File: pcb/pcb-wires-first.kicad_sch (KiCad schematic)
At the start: 54 parts, among them J1 Conn_01x04, J2 Conn_01x04, J3 Conn_01x04, J4 Conn_01x02, J5 Conn_01x02, J6 Conn_01x02, J7 Conn_01x02, SW1 on-1, SW2 off-1, SW3 on-2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

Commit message: More routing.
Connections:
- net fault: now also R4.1
- net switch-3: no longer R4.1
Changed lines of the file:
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@@
 		)
 	)
-	(global_label "switch-3"
+	(global_label "fault"
 		(shape input)
 		(at 290.83 210.82 90)
@@
 		)
 		(property "Intersheetrefs" "${INTERSHEET_REFS}"
-			(at 290.83 199.1262 90)
+			(at 290.83 203.4202 90)
 			(hide yes)
 			(show_name no)

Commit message: Routed!
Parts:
- removed NT2: gnd-bridge, symbol Device:NetTie_2
- added JP1: SolderJumper_2_Bridged, Jumper:SolderJumper-2_P1.3mm_Bridged_RoundedPad1.0x1.5mm, symbol Jumper:SolderJumper_2_Bridged
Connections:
- net GND: now also JP1.2 (B)
- net HV-GND: now also JP1.1 (A)
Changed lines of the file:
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@@
+	(wire
+		(pts
+			(xy 306.07 176.53) (xy 306.07 179.07)
+		)
+		(stroke
+			(width 0)
+			(type default)
+		)
+	)
 	(wire
 		(pts
@@
 	(wire
 		(pts
+			(xy 313.69 179.07) (xy 313.69 176.53)
+		)
+		(stroke
+			(width 0)
+			(type default)
+		)
+	)
+	(wire
+		(pts
 			(xy 134.62 208.28) (xy 132.08 208.28)
 		)
@@
 		(pts
 			(xy 290.83 210.82) (xy 290.83 213.36)
+		)
+		(stroke
+			(width 0)
+			(type default)
+		)
+	)
+	(wire
+		(pts
+			(xy 313.69 176.53) (xy 316.23 176.53)
 		)
 		(stroke
@@
 	)
 	(symbol
-		(lib_id "Device:NetTie_2")
-		(at 311.15 179.07 0)
-		(unit 1)
-		(body_style 1)
-		(exclude_from_sim no)
-		(in_bom no)
-		(on_board yes)
-		(in_pos_files yes)
-		(dnp no)
-		(fields_autoplaced yes)
-		(property "Reference" "NT2"
-			(at 311.15 173.99 0)
-			(hide yes)
-			(show_name no)
-			(do_not_autoplace no)
-			(effects
-				(font
-					(size 1.27 1.27)
-				)
-			)
-		)
-		(property "Value" "gnd-bridge"
-			(at 311.15 176.53 0)
-			(hide yes)
-			(show_name no)
-			(do_not_autoplace no)
-			(effects
-				(font
-					(size 1.27 1.27)
-				)
-			)
-		)
-		(property "Footprint" ""
-			(at 311.15 179.07 0)
-			(hide yes)
-			(show_name no)
-			(do_not_autoplace no)
-			(effects
-				(font
-					(size 1.27 1.27)
-				)
-			)
-		)
-		(property "Datasheet" ""
-			(at 311.15 179.07 0)
-			(hide yes)
-			(show_name no)
-			(do_not_autoplace no)
-			(effects
-				(font
-					(size 1.27 1.27)
-				)
-			)
-		)
-		(property "Description" "Net tie, 2 pins"
-			(at 311.15 179.07 0)
-			(hide yes)
-			(show_name no)
-			(do_not_autoplace no)
-			(effects
-				(font
-					(size 1.27 1.27)
-				)
-			)
-		)
-		(pin "2"
-		)
-		(pin "1"
-		)
-		(instances
-			(project "pcb-wires-first"
-				(path "/2155cca2-5ec1-4d94-9553-ebcda519e5b5"
-					(reference "NT2")
-					(unit 1)
-				)
-			)
-		)
-	)
-	(symbol
 		(lib_id "Device:LED")
 		(at 325.12 226.06 90)
@@
 					(unit 1)
 				)
+			)
+		)
+	)
+	(symbol
+		(lib_id "Jumper:SolderJumper_2_Bridged")
+		(at 311.15 176.53 0)
+		(unit 1)
+		(body_style 1)
+		(exclude_from_sim no)
+		(in_bom no)
+		(on_board yes)
+		(in_pos_files yes)
+		(dnp no)
+		(fields_autoplaced yes)
+		(property "Reference" "JP1"
+			(at 311.15 170.18 0)
+			(show_name no)
+			(do_not_autoplace no)
+			(effects
+				(font
+					(size 1.27 1.27)
+				)
+			)
+		)
+		(property "Value" "SolderJumper_2_Bridged"
+			(at 311.15 172.72 0)
+			(show_name no)
+			(do_not_autoplace no)
+			(effects
+				(font
+					(size 1.27 1.27)
+				)
+			)
+		)
+		(property "Footprint" "Jumper:SolderJumper-2_P1.3mm_Bridged_RoundedPad1.0x1.5mm"
+			(at 311.15 176.53 0)
+			(show_name no)
+			(do_not_autoplace no)
+			(effects
+				(font
+					(size 1.27 1.27)
+				)
+			)
+		)
+		(property "Datasheet" ""
+			(at 311.15 182.88 0)
+			(hide yes)
+			(show_name no)
+			(do_not_autoplace no)
+			(effects
+				(font
+					(size 1.27 1.27)
+				)
+			)
+		)
+		(property "Description" "Solder Jumper, 2-pole, closed/bridged"
+			(at 311.15 181.61 0)
+			(hide yes)
+			(show_name no)
+			(do_not_autoplace no)
+			(effects
+				(font
+					(size 1.27 1.27)
+				)
+			)
+		)
+		(pin "2"
+		)
+		(pin "1"
+		)
+		(instances
+			(project "pcb-wires-first"
+				(path "/2155cca2-5ec1-4d94-9553-ebcda519e5b5"
+					(reference "JP1")
+					(unit 1)
+				)

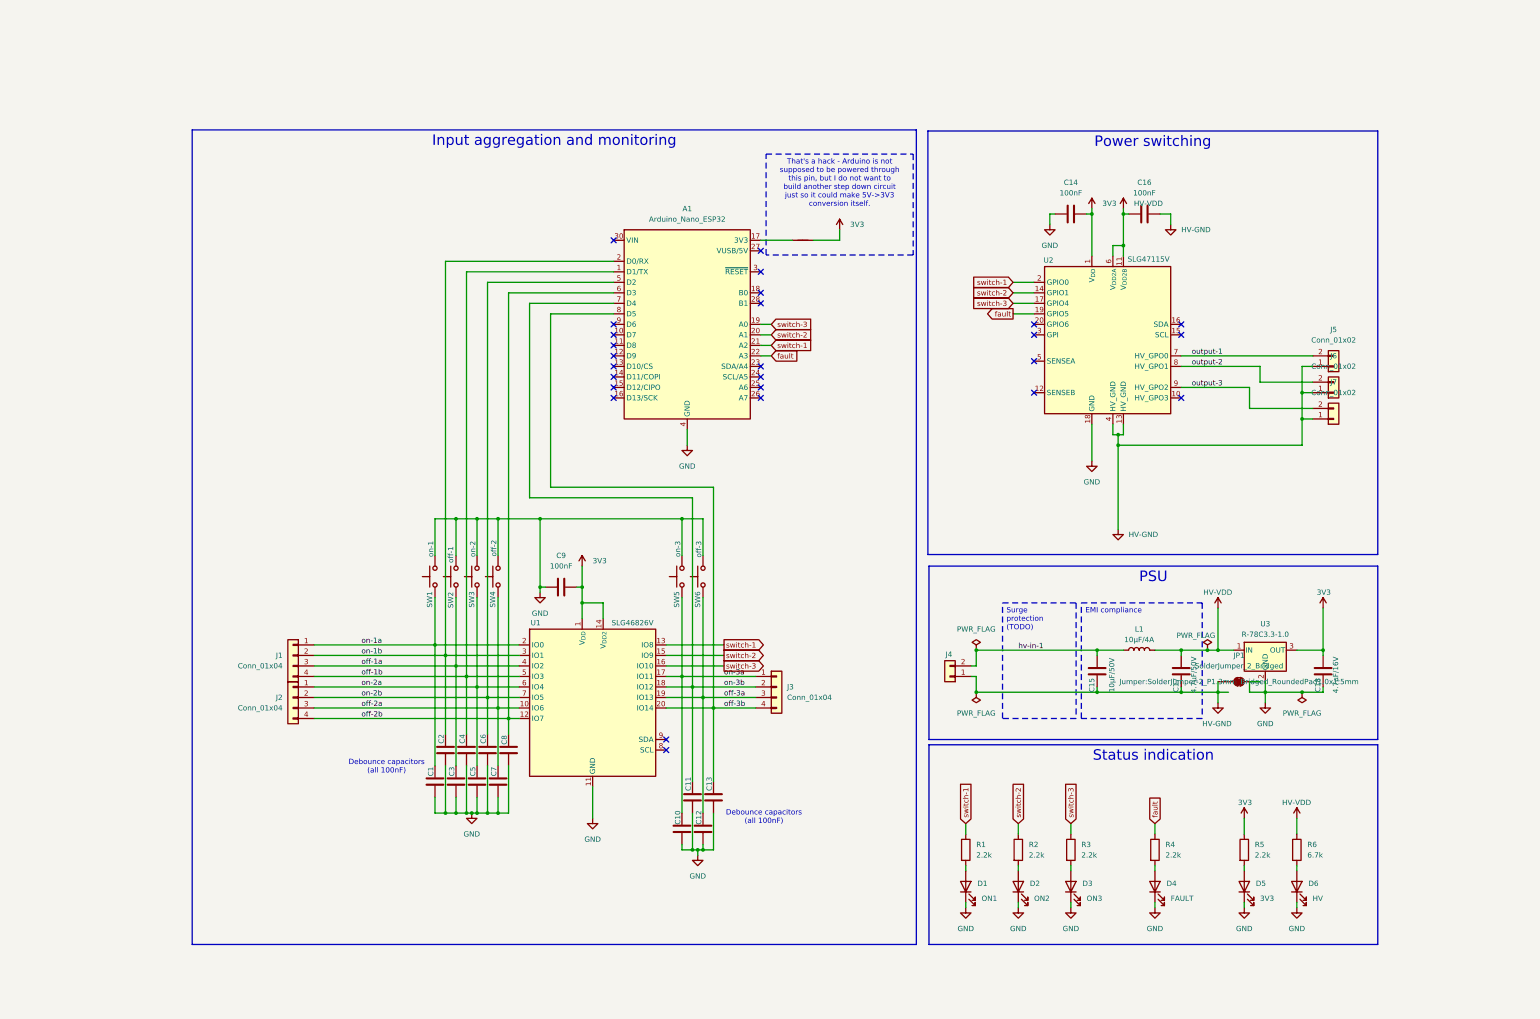
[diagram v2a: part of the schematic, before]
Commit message: Adding an I2C connector.
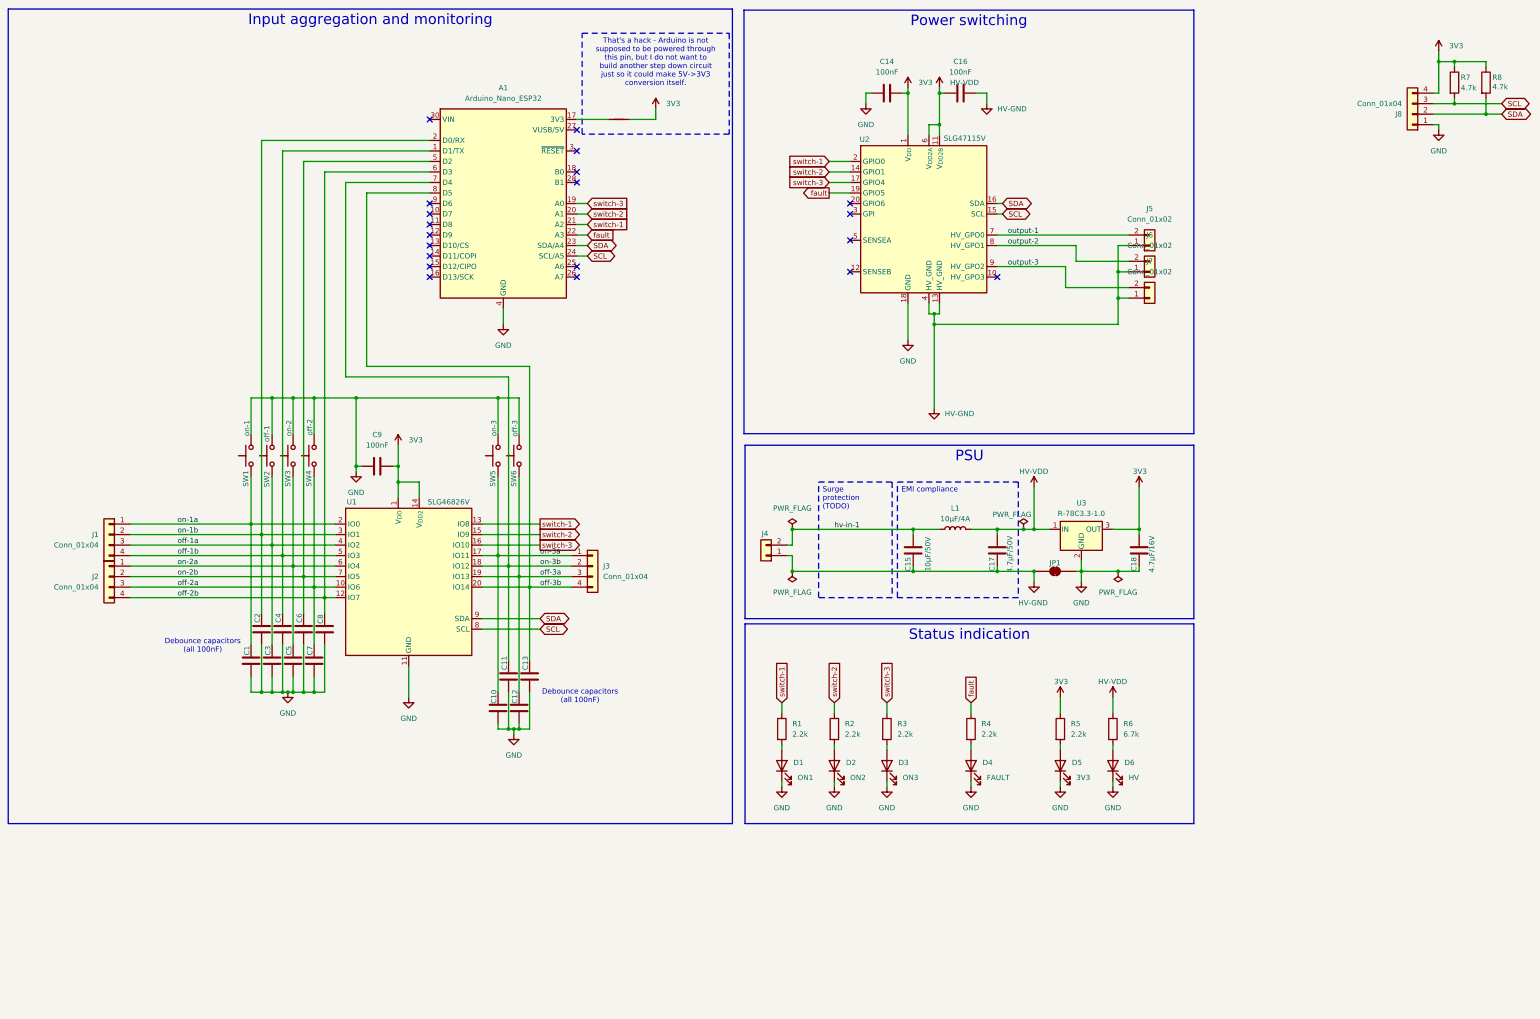
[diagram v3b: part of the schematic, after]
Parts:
- added J8: Conn_01x04, Connector_JST:JST_XH_B4B-XH-A_1x04_P2.50mm_Vertical, symbol Connector_Generic:Conn_01x04
- added R7, R8: 4.7k, Resistor_SMD:R_0603_1608Metric, symbol Device:R
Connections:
- net 3V3: now also J8.4 (Pin_4), R7.1, R8.1
- net GND: now also J8.1 (Pin_1)
- net SDA: now reaches A1.23 (SDA/A4)
- net SDA: now also U1.9 (SDA), U2.16 (SDA), J8.2 (Pin_2), R8.2
- net SCL: now reaches A1.24 (SCL/A5)
- net SCL: now also U1.8 (SCL), U2.15 (SCL), J8.3 (Pin_3), R7.2
- no-connect marks 26 -> 20
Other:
- moved on the sheet: A1, C1, C10, C11, C12, C13, C14, C15, C16, C17, C18, C2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

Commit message: Doing a draft release.
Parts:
- J5, J6, J7: footprint Connector_JST:JST_VH_B2P-VH-FB-B_1x02_P3.96mm_Vertical -> Connector_JST:JST_VH_B2P-VH_1x02_P3.96mm_Vertical
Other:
- moved on the sheet: J8, R7, R8
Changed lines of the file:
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@@
 		(exclude_from_sim no)
 		(at 191.77 119.38 0)
-		(size 108.458 41.91)
+		(size 108.458 40.64)
 		(margins 0.9525 0.9525 0.9525 0.9525)
 		(stroke
@@
 		)
 	)
+	(text_box "I2C"
+		(exclude_from_sim no)
+		(at 302.26 13.97 0)
+		(size 104.14 44.45)
+		(margins 0.9525 0.9525 0.9525 0.9525)
+		(stroke
+			(width 0)
+			(type solid)
+		)
+		(fill
+			(type none)
+		)
+		(effects
+			(font
+				(size 2.54 2.54)
+			)
+			(justify top)
+		)
+	)
 	(junction
 		(at 238.76 41.91)
@@
 	)
 	(junction
-		(at 363.22 26.67)
+		(at 363.22 29.21)
 		(diameter 0)
 		(color 0 0 0 0)
 	)
 	(junction
-		(at 363.22 36.83)
+		(at 363.22 39.37)
 		(diameter 0)
 		(color 0 0 0 0)
@@
 	)
 	(junction
-		(at 370.84 39.37)
+		(at 370.84 41.91)
 		(diameter 0)
 		(color 0 0 0 0)
@@
 	)
 	(junction
-		(at 359.41 26.67)
+		(at 359.41 29.21)
 		(diameter 0)
 		(color 0 0 0 0)
@@
 	(wire
 		(pts
-			(xy 358.14 34.29) (xy 359.41 34.29)
+			(xy 358.14 36.83) (xy 359.41 36.83)
 		)
 		(stroke
@@
 	(wire
 		(pts
-			(xy 363.22 27.94) (xy 363.22 26.67)
+			(xy 363.22 30.48) (xy 363.22 29.21)
 		)
 		(stroke
@@
 	(wire
 		(pts
-			(xy 363.22 26.67) (xy 359.41 26.67)
+			(xy 363.22 29.21) (xy 359.41 29.21)
 		)
 		(stroke
@@
 	(wire
 		(pts
-			(xy 359.41 26.67) (xy 359.41 24.13)
+			(xy 359.41 29.21) (xy 359.41 26.67)
 		)
 		(stroke
@@
 	(wire
 		(pts
-			(xy 358.14 36.83) (xy 363.22 36.83)
+			(xy 358.14 39.37) (xy 363.22 39.37)
 		)
 		(stroke
@@
 	(wire
 		(pts
-			(xy 359.41 34.29) (xy 359.41 26.67)
+			(xy 359.41 36.83) (xy 359.41 29.21)
 		)
 		(stroke
@@
 	(wire
 		(pts
-			(xy 363.22 36.83) (xy 374.65 36.83)
+			(xy 363.22 39.37) (xy 374.65 39.37)
 		)
 		(stroke
@@
 	(wire
 		(pts
-			(xy 370.84 27.94) (xy 370.84 26.67)
+			(xy 370.84 30.48) (xy 370.84 29.21)
 		)
 		(stroke
@@
 	(wire
 		(pts
-			(xy 363.22 35.56) (xy 363.22 36.83)
+			(xy 363.22 38.1) (xy 363.22 39.37)
 		)
 		(stroke
@@
 	(wire
 		(pts
-			(xy 370.84 39.37) (xy 374.65 39.37)
+			(xy 370.84 41.91) (xy 374.65 41.91)
 		)
 		(stroke
@@
 	(wire
 		(pts
-			(xy 358.14 41.91) (xy 359.41 41.91)
+			(xy 358.14 44.45) (xy 359.41 44.45)
 		)
 		(stroke
@@
 	(wire
 		(pts
-			(xy 370.84 26.67) (xy 363.22 26.67)
+			(xy 370.84 29.21) (xy 363.22 29.21)
 		)
 		(stroke
@@
 	(wire
 		(pts
-			(xy 358.14 39.37) (xy 370.84 39.37)
+			(xy 358.14 41.91) (xy 370.84 41.91)
 		)
 		(stroke
@@
 	(wire
 		(pts
-			(xy 370.84 35.56) (xy 370.84 39.37)
+			(xy 370.84 38.1) (xy 370.84 41.91)
 		)
 		(stroke
@@
 	(wire
 		(pts
-			(xy 359.41 41.91) (xy 359.41 43.18)
+			(xy 359.41 44.45) (xy 359.41 45.72)
 		)
 		(stroke
@@
 	(global_label "SCL"
 		(shape bidirectional)
-		(at 374.65 36.83 0)
+		(at 374.65 39.37 0)
 		(fields_autoplaced yes)
 		(effects
@@
 		)
 		(property "Intersheetrefs" "${INTERSHEET_REFS}"
-			(at 382.2541 36.83 0)
+			(at 382.2541 39.37 0)
 			(hide yes)
 			(show_name no)
@@
 	(global_label "SDA"
 		(shape bidirectional)
-		(at 374.65 39.37 0)
+		(at 374.65 41.91 0)
 		(fields_autoplaced yes)
 		(effects
@@
 		)
 		(property "Intersheetrefs" "${INTERSHEET_REFS}"
-			(at 382.3146 39.37 0)
+			(at 382.3146 41.91 0)
 			(hide yes)
 			(show_name no)
@@
 	(symbol
 		(lib_id "power:GND")
-		(at 359.41 43.18 0)
+		(at 359.41 45.72 0)
 		(unit 1)
 		(body_style 1)
@@
 		(fields_autoplaced yes)
 		(property "Reference" "#PWR026"
-			(at 359.41 49.53 0)
+			(at 359.41 52.07 0)
 			(hide yes)
 			(show_name no)
@@
 		)
 		(property "Value" "GND"
-			(at 359.41 48.26 0)
+			(at 359.41 50.8 0)
 			(show_name no)
 			(do_not_autoplace no)
@@
 		)
 		(property "Footprint" ""
-			(at 359.41 43.18 0)
+			(at 359.41 45.72 0)
 			(hide yes)
 			(show_name no)
@@
 		)
 		(property "Datasheet" ""
-			(at 359.41 43.18 0)
+			(at 359.41 45.72 0)
 			(hide yes)
 			(show_name no)
@@
 		)
 		(property "Description" "Power symbol creates a global label with name \"GND\" , ground"
-			(at 359.41 43.18 0)
+			(at 359.41 45.72 0)
 			(hide yes)
 			(show_name no)
@@
 	(symbol
 		(lib_id "Connector_Generic:Conn_01x04")
-		(at 353.06 39.37 180)
+		(at 353.06 41.91 180)
 		(unit 1)
 		(body_style 1)
@@
 		(dnp no)
 		(property "Reference" "J8"
-			(at 350.52 39.3701 0)
+			(at 350.52 41.9101 0)
 			(show_name no)
 			(do_not_autoplace no)
@@
 		)
 		(property "Value" "Conn_01x04"
-			(at 350.52 36.8301 0)
+			(at 350.52 39.3701 0)
 			(show_name no)
 			(do_not_autoplace no)
@@
 		)
 		(property "Footprint" "Connector_JST:JST_XH_B4B-XH-A_1x04_P2.50mm_Vertical"
-			(at 353.06 39.37 0)
+			(at 353.06 41.91 0)
 			(hide yes)
 			(show_name no)
@@
 		)
 		(property "Datasheet" ""
-			(at 353.06 39.37 0)
+			(at 353.06 41.91 0)
 			(hide yes)
 			(show_name no)
@@
 		)
 		(property "Description" "Generic connector, single row, 01x04, script generated (kicad-library-utils/schlib/autogen/connector/)"
-			(at 353.06 39.37 0)
+			(at 353.06 41.91 0)
 			(hide yes)
 			(show_name no)
@@
 	(symbol
 		(lib_id "Device:R")
-		(at 370.84 31.75 0)
+		(at 370.84 34.29 0)
 		(unit 1)
 		(body_style 1)
@@
 		(dnp no)
 		(property "Reference" "R8"
-			(at 372.364 30.48 0)
+			(at 372.364 33.02 0)
 			(show_name no)
 			(do_not_autoplace no)
@@
 		)
 		(property "Value" "4.7k"
-			(at 372.364 32.766 0)
+			(at 372.364 35.306 0)
 			(show_name no)
 			(do_not_autoplace no)
@@
 		)
 		(property "Footprint" "Resistor_SMD:R_0603_1608Metric"
-			(at 369.062 31.75 90)
+			(at 369.062 34.29 90)
 			(hide yes)
 			(show_name no)
@@
 		)
 		(property "Datasheet" ""
-			(at 370.84 31.75 0)
+			(at 370.84 34.29 0)
 			(hide yes)
 			(show_name no)
@@
 		)
 		(property "Description" "Resistor"
-			(at 370.84 31.75 0)
+			(at 370.84 34.29 0)
 			(hide yes)
 			(show_name no)
@@
 	(symbol
 		(lib_id "Device:R")
-		(at 363.22 31.75 0)
+		(at 363.22 34.29 0)
 		(unit 1)
 		(body_style 1)
@@
 		(dnp no)
 		(property "Reference" "R7"
-			(at 364.744 30.48 0)
+			(at 364.744 33.02 0)
 			(show_name no)
 			(do_not_autoplace no)
@@
 		)
 		(property "Value" "4.7k"
-			(at 364.744 33.02 0)
+			(at 364.744 35.56 0)
 			(show_name no)
 			(do_not_autoplace no)
@@
 		)
 		(property "Footprint" "Resistor_SMD:R_0603_1608Metric"
-			(at 361.442 31.75 90)
+			(at 361.442 34.29 90)
 			(hide yes)
 			(show_name no)
@@
 		)
 		(property "Datasheet" ""
-			(at 363.22 31.75 0)
+			(at 363.22 34.29 0)
 			(hide yes)
 			(show_name no)
@@
 		)
 		(property "Description" "Resistor"
-			(at 363.22 31.75 0)
+			(at 363.22 34.29 0)
 			(hide yes)
 			(show_name no)
@@
 			)
 		)
-		(property "Footprint" "Connector_JST:JST_VH_B2P-VH-FB-B_1x02_P3.96mm_Vertical"
+		(property "Footprint" "Connector_JST:JST_VH_B2P-VH_1x02_P3.96mm_Vertical"
 			(at 289.56 71.12 0)
 			(hide yes)
@@
 			)
 		)
-		(property "Footprint" "Connector_JST:JST_VH_B2P-VH-FB-B_1x02_P3.96mm_Vertical"
+		(property "Footprint" "Connector_JST:JST_VH_B2P-VH_1x02_P3.96mm_Vertical"
 			(at 289.56 83.82 0)
 			(hide yes)
@@
 	(symbol
 		(lib_id "power:VDD")
-		(at 359.41 24.13 0)
+		(at 359.41 26.67 0)
 		(unit 1)
 		(body_style 1)
@@
 		(fields_autoplaced yes)
 		(property "Reference" "#PWR027"
-			(at 359.41 27.94 0)
+			(at 359.41 30.48 0)
 			(hide yes)
 			(show_name no)
@@
 		)
 		(property "Value" "3V3"
-			(at 361.95 22.8599 0)
+			(at 361.95 25.3999 0)
 			(show_name no)
 			(do_not_autoplace no)
@@
 		)
 		(property "Footprint" ""
-			(at 359.41 24.13 0)
+			(at 359.41 26.67 0)
 			(hide yes)
 			(show_name no)
@@
 		)
 		(property "Datasheet" ""
-			(at 359.41 24.13 0)
+			(at 359.41 26.67 0)
 			(hide yes)
 			(show_name no)
@@
 		)
 		(property "Description" "Power symbol creates a global label with name \"VDD\""
-			(at 359.41 24.13 0)
+			(at 359.41 26.67 0)
 			(hide yes)
 			(show_name no)
@@
 			)
 		)
-		(property "Footprint" "Connector_JST:JST_VH_B2P-VH-FB-B_1x02_P3.96mm_Vertical"
+		(property "Footprint" "Connector_JST:JST_VH_B2P-VH_1x02_P3.96mm_Vertical"
 			(at 289.56 77.47 0)
 			(hide yes)

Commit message: Adding a custom mounting hole footprint which excludes copper.
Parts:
- H1, H2, H3, H4: footprint MountingHole:MountingHole_3.2mm_M3 -> Local:MountingHole_3.2mm_M3
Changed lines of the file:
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@@
 			)
 		)
-		(property "Footprint" "MountingHole:MountingHole_3.2mm_M3"
+		(property "Footprint" "Local:MountingHole_3.2mm_M3"
 			(at 259.08 273.05 0)
 			(hide yes)
@@
 			)
 		)
-		(property "Footprint" "MountingHole:MountingHole_3.2mm_M3"
+		(property "Footprint" "Local:MountingHole_3.2mm_M3"
 			(at 279.4 278.13 0)
 			(hide yes)
@@
 			)
 		)
-		(property "Footprint" "MountingHole:MountingHole_3.2mm_M3"
+		(property "Footprint" "Local:MountingHole_3.2mm_M3"
 			(at 259.08 278.13 0)
 			(hide yes)
@@
 			)
 		)
-		(property "Footprint" "MountingHole:MountingHole_3.2mm_M3"
+		(property "Footprint" "Local:MountingHole_3.2mm_M3"
 			(at 279.4 273.05 0)
 			(hide yes)

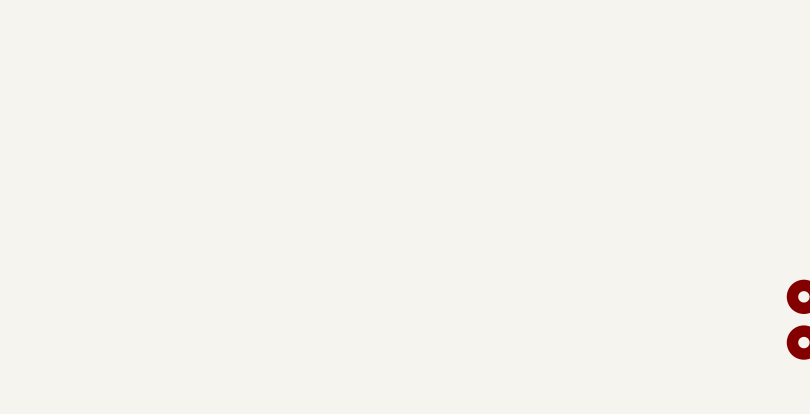
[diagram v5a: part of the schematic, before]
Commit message: Adding more testpoints.
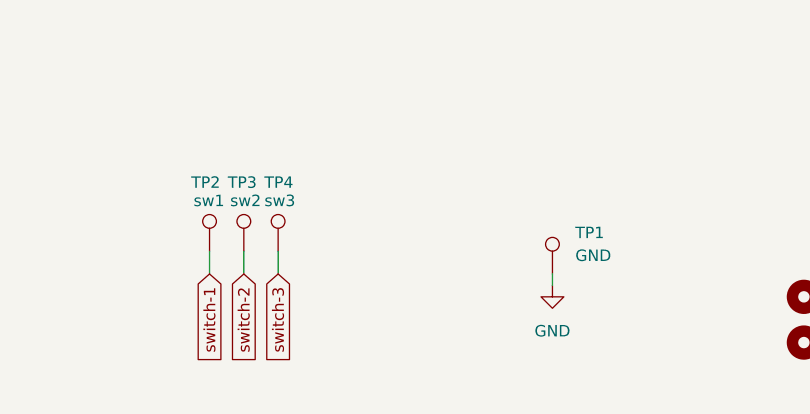
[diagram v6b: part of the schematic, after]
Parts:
- added TP1: GND, TestPoint:TestPoint_Keystone_5019_Miniature, symbol Connector:TestPoint
- added TP2: sw1, TestPoint:TestPoint_Keystone_5010-5014_Multipurpose, symbol Connector:TestPoint
- added TP3: sw2, TestPoint:TestPoint_Keystone_5010-5014_Multipurpose, symbol Connector:TestPoint
- added TP4: sw3, TestPoint:TestPoint_Keystone_5010-5014_Multipurpose, symbol Connector:TestPoint
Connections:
- net GND: now also TP1.1
- net switch-1: now also TP2.1
- net switch-2: now also TP3.1
- net switch-3: now also TP4.1

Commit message: Moving model pusher into a separate project.
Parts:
- J4: footprint Connector_JST:JST_VH_B2P-VH-FB-B_1x02_P3.96mm_Vertical -> Connector_JST:JST_VH_B2P-VH_1x02_P3.96mm_Vertical
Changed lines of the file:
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@@
 			)
 		)
-		(property "Footprint" "Connector_JST:JST_VH_B2P-VH-FB-B_1x02_P3.96mm_Vertical"
+		(property "Footprint" "Connector_JST:JST_VH_B2P-VH_1x02_P3.96mm_Vertical"
 			(at 196.85 146.05 0)
 			(hide yes)

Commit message: Adding notes for vNext.
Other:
- note added: "Issues. 1. Input connectors do not have GND. 2. IO6 and IO7 are GPO on 46826. 3. It is 47105, not 47115. 4. Add blinker LEDs to each SLG."
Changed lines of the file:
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@@
+		)
+	)
+	(text "Issues. 1. Input connectors do not have GND. 2. IO6 and IO7 are GPO on 46826. 3. It is 47105, not 47115. 4. Add blinker LEDs to each SLG."
+		(exclude_from_sim no)
+		(at 273.05 215.138 0)
+		(effects
+			(font
+				(size 1.27 1.27)
+			)
 		)
 	)
